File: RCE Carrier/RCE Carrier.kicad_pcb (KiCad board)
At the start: 2 copper layers, 38 x 39.5 mm, 46 parts, among them J1 TBL002A-350-08GY-2GY, J10 Conn_01x06_Pin, J2 Conn_01x02, J3 Conn_01x02, J5 DF40C-34DP-0.4V_58_, J6 PRT-16766, J7 DF40C-34DP-0.4V_58_, Q5 SI7232DN-T1-GE3, Q6 SI7232DN-T1-GE3, U1 TPS75533KTTRG3, U2 NCP1117-3.3_SOT223, U6 LM293, U7 LM293

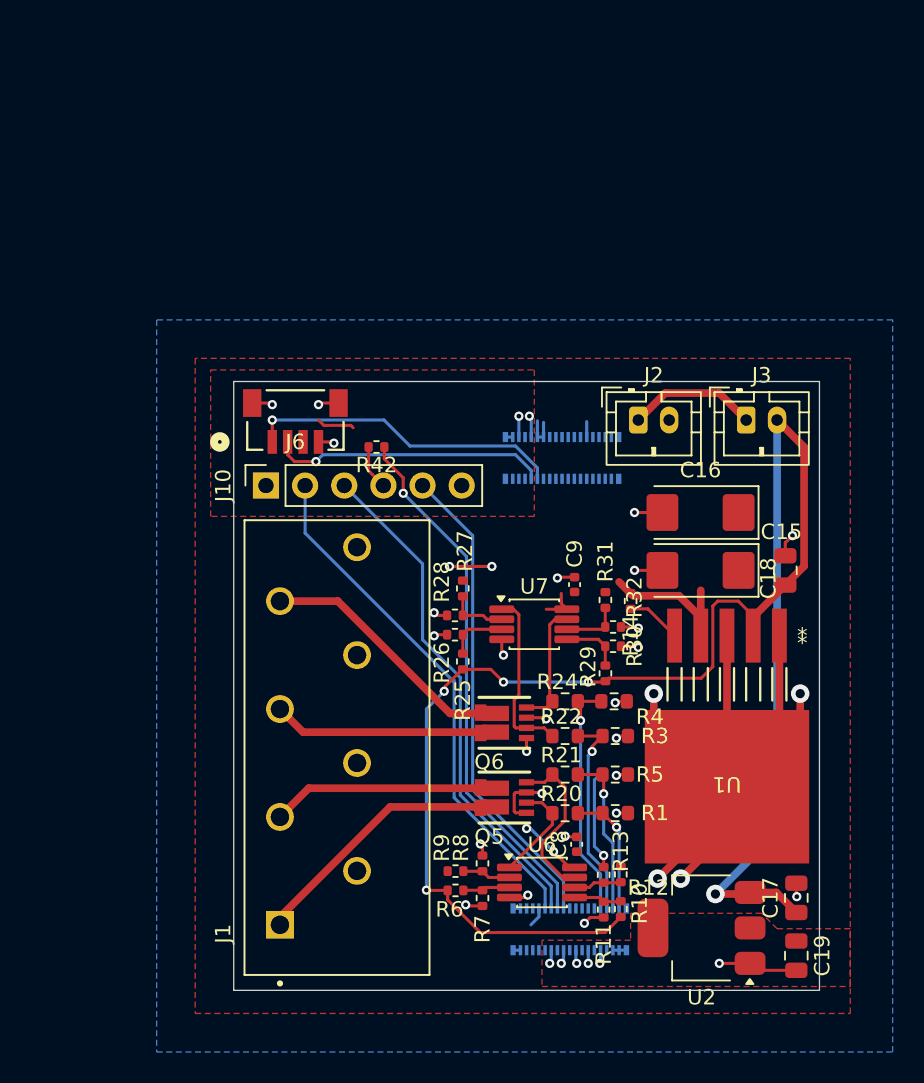
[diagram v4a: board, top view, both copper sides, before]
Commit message: RCE silkscreen + rounding corners
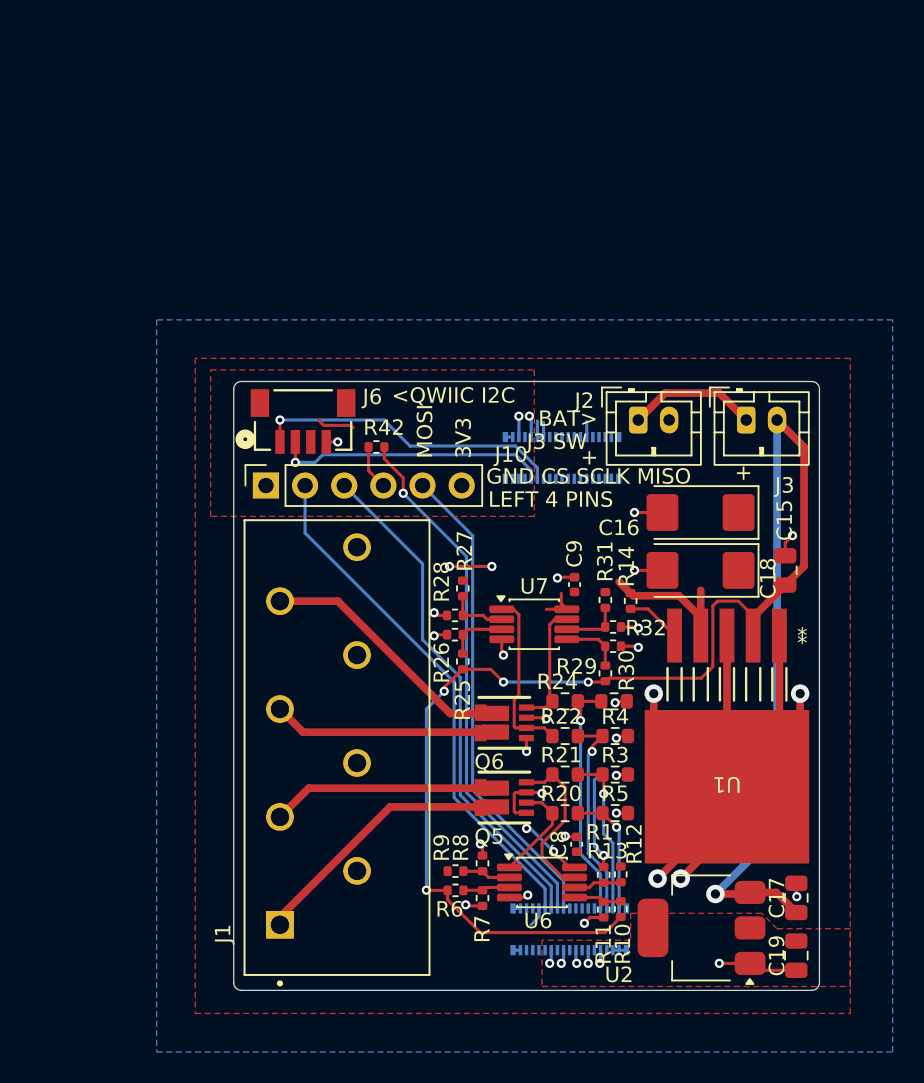
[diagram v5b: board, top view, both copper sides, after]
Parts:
- added G***: LOGO, WURocketry_logo:WURocketry_logo, B.Cu at (156.5, 84.5)
- moved J6 0.50 mm to (132.0, 79.0)
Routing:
- net GND: track 104.3 -> 101.3 mm, vias 33 -> 31
- net /SCL: track 20.6 -> 20.1 mm
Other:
- outline, holes or cut-outs redrawn
- board text added: "+"
- board text added: "3V3"
- board text added: "<QWIIC I2C"
- board text added: "BAT>"
- board text added: "Carrier"
- board text added: "Department of Electrical and Systems Engineering Washington University McKelvey School of Engineering"
- board text added: "GND CS SCLK MISO"
- board text added: "J3 SW"
- board text added: "LEFT 4 PINS"
- board text added: "MOSI"
- board text added: "PYRO 1"
- board text added: "PYRO 2"
- board text added: "PYRO 3"
- board text added: "PYRO 4"
- board text added: "RCE"
- board text added: "WURocketry 2026-2027"
- board text added: "for Airdahl Flight Computer"

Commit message: DRC changes and updated fab files
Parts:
- J10: footprint Connector_PinSocket_2.54mm:PinSocket_1x06_P2.54mm_Vertical -> Connector_PinHeader_2.54mm:PinHeader_1x06_P2.54mm_Vertical
- R1: value 3.3k -> 1k
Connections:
- J6 pad 5: (no net) -> GND
- J6 pad 6: (no net) -> GND
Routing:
- net GND: track 101.3 -> 107.8 mm, vias 31 -> 33
- net +3.3V/BP: track 17.0 -> 18.5 mm

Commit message: silkscreen shenanigans
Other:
- board text added: "through roaring flames and skies of blue sensors sharp, tracking through apogee's peak firing charges when the time is right oh **** did i remove the flight tags"
- board text added: "{dblquote}feel the breeze{dblquote}"
- board text added: "{dblquote}ground is ground{dblquote}"
- board text added: "{dblquote}it'll take only 30 min{dblquote}"
- board text added: "{dblquote}mack stinks{dblquote}"
- board text added: "{dblquote}plug and suffer{dblquote}"
- board text added: "{dblquote}the rocket went to heaven{dblquote}"
- board text added: "{dblquote}why did i do that?"
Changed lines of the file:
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@@
 			(at 2.1375 0.075 180)
 			(layer "F.SilkS")
+			(hide yes)
 			(effects
 				(font
@@
 			(at 0.8525 2.175 90)
 			(layer "F.SilkS")
+			(hide yes)
 			(effects
 				(font
@@
 		(at 130.5 111.75 90)
 		(property "Reference" "J1"
-			(at -0.575 -3.685 90)
+			(at -2.55 10.8 90)
 			(layer "F.SilkS")
 			(effects
@@
 			(at 0.9762 -2.53811 0)
 			(layer "F.SilkS")
+			(hide yes)
 			(effects
 				(font
@@
 			(at 0 1.25 0)
 			(layer "F.SilkS")
+			(hide yes)
 			(effects
 				(font
@@
 			(at 2.24 0 90)
 			(layer "F.SilkS")
+			(hide yes)
 			(effects
 				(font
@@
 			(at -0.25 -1.26 0)
 			(layer "F.SilkS")
+			(hide yes)
 			(effects
 				(font
@@
 			(at 0.9762 -2.53811 0)
 			(layer "F.SilkS")
+			(hide yes)
 			(effects
 				(font
@@
 			(at -2.425 -0.1375 90)
 			(layer "F.SilkS")
+			(hide yes)
 			(effects
 				(font
@@
 			(at 3.255916 -0.03252 90)
 			(layer "F.SilkS")
+			(hide yes)
 			(effects
 				(font
@@
 			(at -2.5 0 90)
 			(layer "F.SilkS")
+			(hide yes)
 			(effects
 				(font
@@
 			(at 2.01 0 90)
 			(layer "F.SilkS")
+			(hide yes)
 			(effects
 				(font
@@
 			(at 0 -1.25 90)
 			(layer "F.SilkS")
+			(hide yes)
 			(effects
 				(font
@@
 			(at 0.435 -1.8625 180)
 			(layer "F.SilkS")
+			(hide yes)
 			(effects
 				(font
@@
 			(at 0.075 1 0)
 			(layer "F.SilkS")
+			(hide yes)
 			(effects
 				(font
@@
 			(at 1.015 -1.3875 90)
 			(layer "F.SilkS")
+			(hide yes)
 			(effects
 				(font
@@
 			(at 0 -1.16 90)
 			(layer "F.SilkS")
+			(hide yes)
 			(effects
 				(font
@@
 			(at -0.5 -1.26 0)
 			(layer "F.SilkS")
+			(hide yes)
 			(effects
 				(font
@@
 			(at -0.25 -1.26 0)
 			(layer "F.SilkS")
+			(hide yes)
 			(effects
 				(font
@@
 			(at -2.275 0.1375 90)
 			(layer "F.SilkS")
+			(hide yes)
 			(effects
 				(font
@@
 			(unlocked yes)
 			(layer "F.SilkS")
+			(hide yes)
 			(effects
 				(font
@@
 			(at -0.25 2.5 0)
 			(layer "F.SilkS")
+			(hide yes)
 			(effects
 				(font
@@
 			(at 0 1.25 0)
 			(layer "F.SilkS")
+			(hide yes)
 			(effects
 				(font
@@
 			(at -2.51 0 90)
 			(layer "F.SilkS")
+			(hide yes)
 			(effects
 				(font
@@
 			(at 2 0 90)
 			(layer "F.SilkS")
+			(hide yes)
 			(effects
 				(font
@@
 			(at 5.35 -3.05 0)
 			(layer "F.SilkS")
+			(hide yes)
 			(effects
 				(font
@@
 			(at -0.49 1.25 0)
 			(layer "F.SilkS")
+			(hide yes)
 			(effects
 				(font
@@
 			(at -2.24 0.25 90)
 			(layer "F.SilkS")
+			(hide yes)
 			(effects
 				(font
@@
 			(at -0.3875 1.235 0)
 			(layer "F.SilkS")
+			(hide yes)
 			(effects
 				(font
@@
 			(at -0.25 -1.26 0)
 			(layer "F.SilkS")
+			(hide yes)
 			(effects
 				(font
@@
 			(at 1.535 0.25 180)
 			(layer "F.SilkS")
+			(hide yes)
 			(effects
 				(font
@@
 			(at 5.28252 -1 0)
 			(layer "F.SilkS")
+			(hide yes)
 			(effects
 				(font
@@
 			(at -1.975 -0.8875 90)
 			(layer "F.SilkS")
+			(hide yes)
 			(effects
 				(font
@@
 			(at 0 1.25 90)
 			(layer "F.SilkS")
+			(hide yes)
 			(effects
 				(font
@@
 			(at -0.8875 -1.515 90)
 			(layer "F.SilkS")
+			(hide yes)
 			(effects
 				(font
@@
 			(at -4.399998 -0.5151 90)
 			(layer "F.SilkS")
+			(hide yes)
 			(effects
 				(font
@@
 			(at -1 1.25 0)
 			(layer "F.SilkS")
+			(hide yes)
 			(effects
 				(font
@@
 			(at 0.8525 -1.825 90)
 			(layer "F.SilkS")
+			(hide yes)
 			(effects
 				(font
@@
 			(at 0.8875 1.575 270)
 			(layer "F.SilkS")
+			(hide yes)
 			(effects
 				(font
@@
 			(at 0 -2.45 0)
 			(layer "F.SilkS")
+			(hide yes)
 			(effects
 				(font
@@
 		(layer "Edge.Cuts")
 	)
+	(gr_text "{dblquote}feel the breeze{dblquote}"
+		(at 141.1 106.4 0)
+		(layer "F.SilkS")
+		(effects
+			(font
+				(size 0.5 0.5)
+			)
+			(justify left bottom)
+		)
+	)
+	(gr_text "{dblquote}why did i do that?"
+		(at 143.3 95.3 0)
+		(layer "F.SilkS")
+		(effects
+			(font
+				(size 0.5 0.5)
+			)
+			(justify left bottom)
+		)
+	)
+	(gr_text "{dblquote}the rocket\nwent to heaven{dblquote}"
+		(at 143.5 112.6 0)
+		(layer "F.SilkS")
+		(effects
+			(font
+				(size 0.5 0.5)
+			)
+			(justify left bottom)
+		)
+	)
+	(gr_text "{dblquote}it'll take only\n30 min{dblquote}"
+		(at 149.2 86 180)
+		(layer "F.SilkS")
+		(effects
+			(font
+				(size 0.5 0.5)
+			)
+			(justify left bottom)
+		)
+	)
+	(gr_text "{dblquote}ground is ground{dblquote}"
+		(at 150 114.8 180)
+		(layer "F.SilkS")
+		(effects
+			(font
+				(size 0.5 0.5)
+			)
+			(justify left bottom)
+		)
+	)
+	(gr_text "{dblquote}plug and suffer{dblquote}"
+		(at 141.4 97.5 270)
+		(layer "F.SilkS")
+		(effects
+			(font
+				(size 0.5 0.5)
+			)
+			(justify left bottom)
+		)
+	)
+	(gr_text "{dblquote}mack \nstinks{dblquote}"
+		(at 151.1 85.6 270)
+		(layer "F.SilkS")
+		(effects
+			(font
+				(size 0.5 0.5)
+			)
+			(justify left bottom)
+		)
+	)
 	(gr_text "<QWIIC I2C"
 		(at 137.75 78 0)
@@
 		)
 	)
+	(gr_text "through roaring flames and skies of blue\nsensors sharp, tracking through apogee's peak\nfiring charges when the time is right\noh **** did i remove the flight tags"
+		(at 161.6 102 0)
+		(layer "B.SilkS")
+		(effects
+			(font
+				(size 0.75 0.75)
+				(thickness 0.075)
+			)
+			(justify left bottom mirror)
+		)
+	)
 	(gr_text "WURocketry 2026-2027"
 		(at 165 115.5 0)
@@
 	)
 	(gr_text "PYRO 4"
-		(at 132.25 93.5 270)
+		(at 132.4 91.5 270)
 		(layer "B.SilkS")
 		(effects
@@
 	)
 	(gr_text "PYRO 3"
-		(at 132.25 100.5 270)
+		(at 132.4 98.5 270)
 		(layer "B.SilkS")
 		(effects
@@
 	)
 	(gr_text "PYRO 2"
-		(at 132.25 107.5 270)
+		(at 132.5 105.6 270)
 		(layer "B.SilkS")
 		(effects
@@
 	)
 	(gr_text "PYRO 1"
-		(at 132.25 114.25 270)
+		(at 132.6 113 270)
 		(layer "B.SilkS")
 		(effects
